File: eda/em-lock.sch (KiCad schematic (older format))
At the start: 47 parts, among them P1 EXT_LED_CONN, P2 RC522A, P3 RC522B, P4 BTN_OPEN, P5 BTN_CALL, P6 ESP8266_CONN, P7 LOCK_CONN, Q1 MMBT3906, Q2 MMBT3906, Q3 MMBT3906, Q4 Q_NMOS_DGS, U1 74LVC2G14

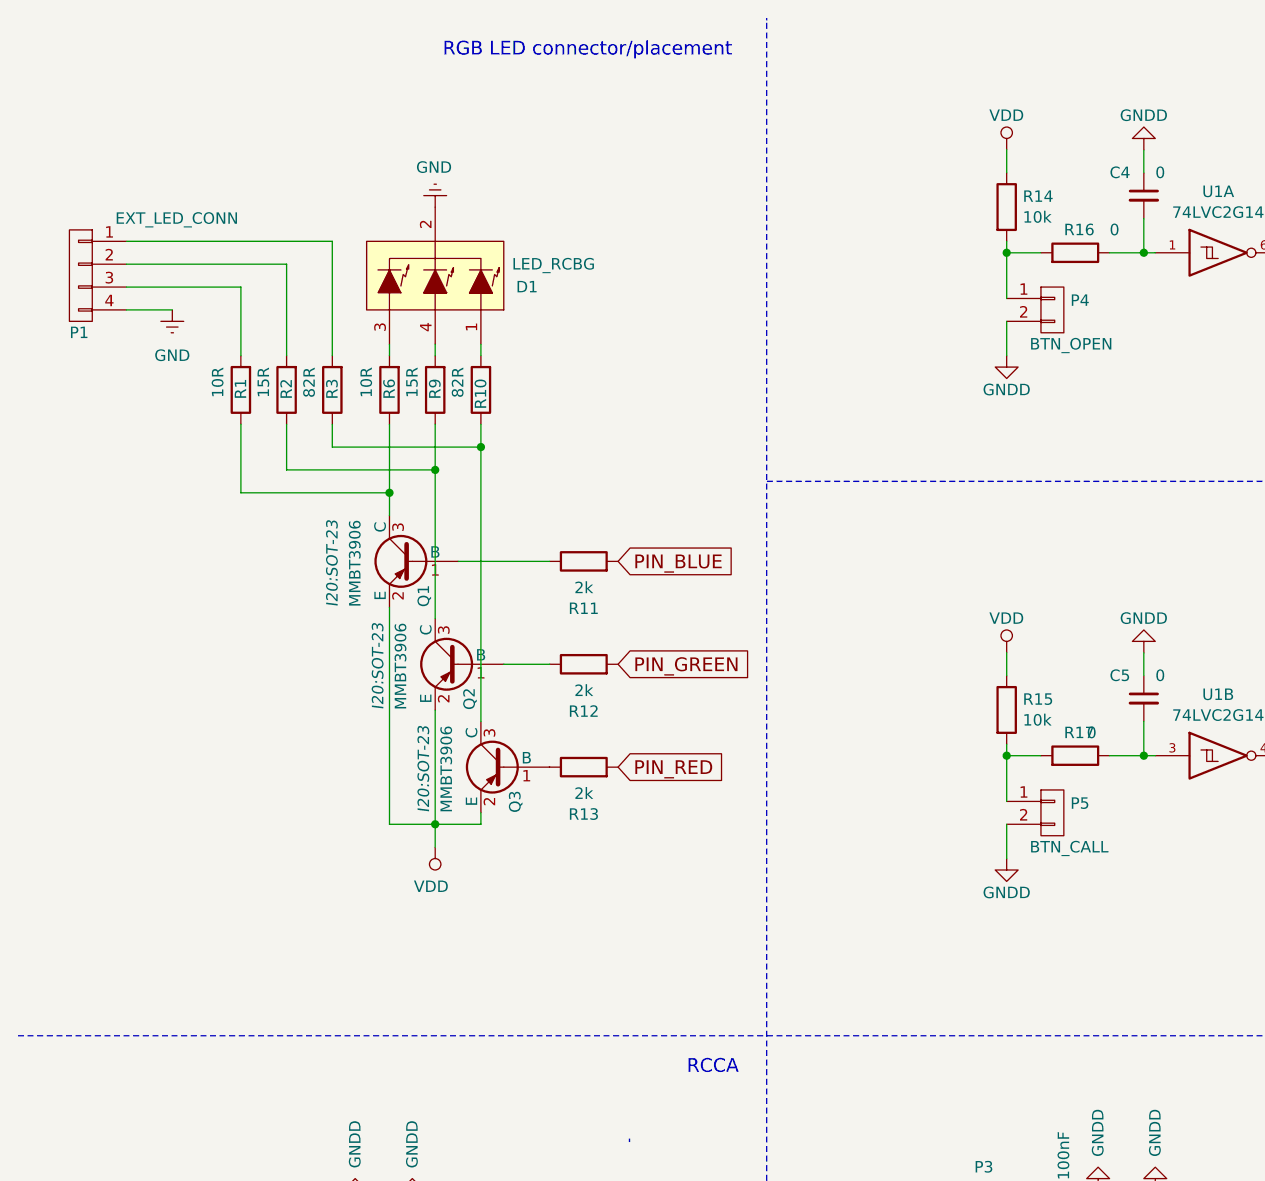
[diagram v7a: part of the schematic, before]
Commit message: refs #41563 rc522 moved up, RGB LEDs moved to separate pcbs, 3d model of rc522 implemented.
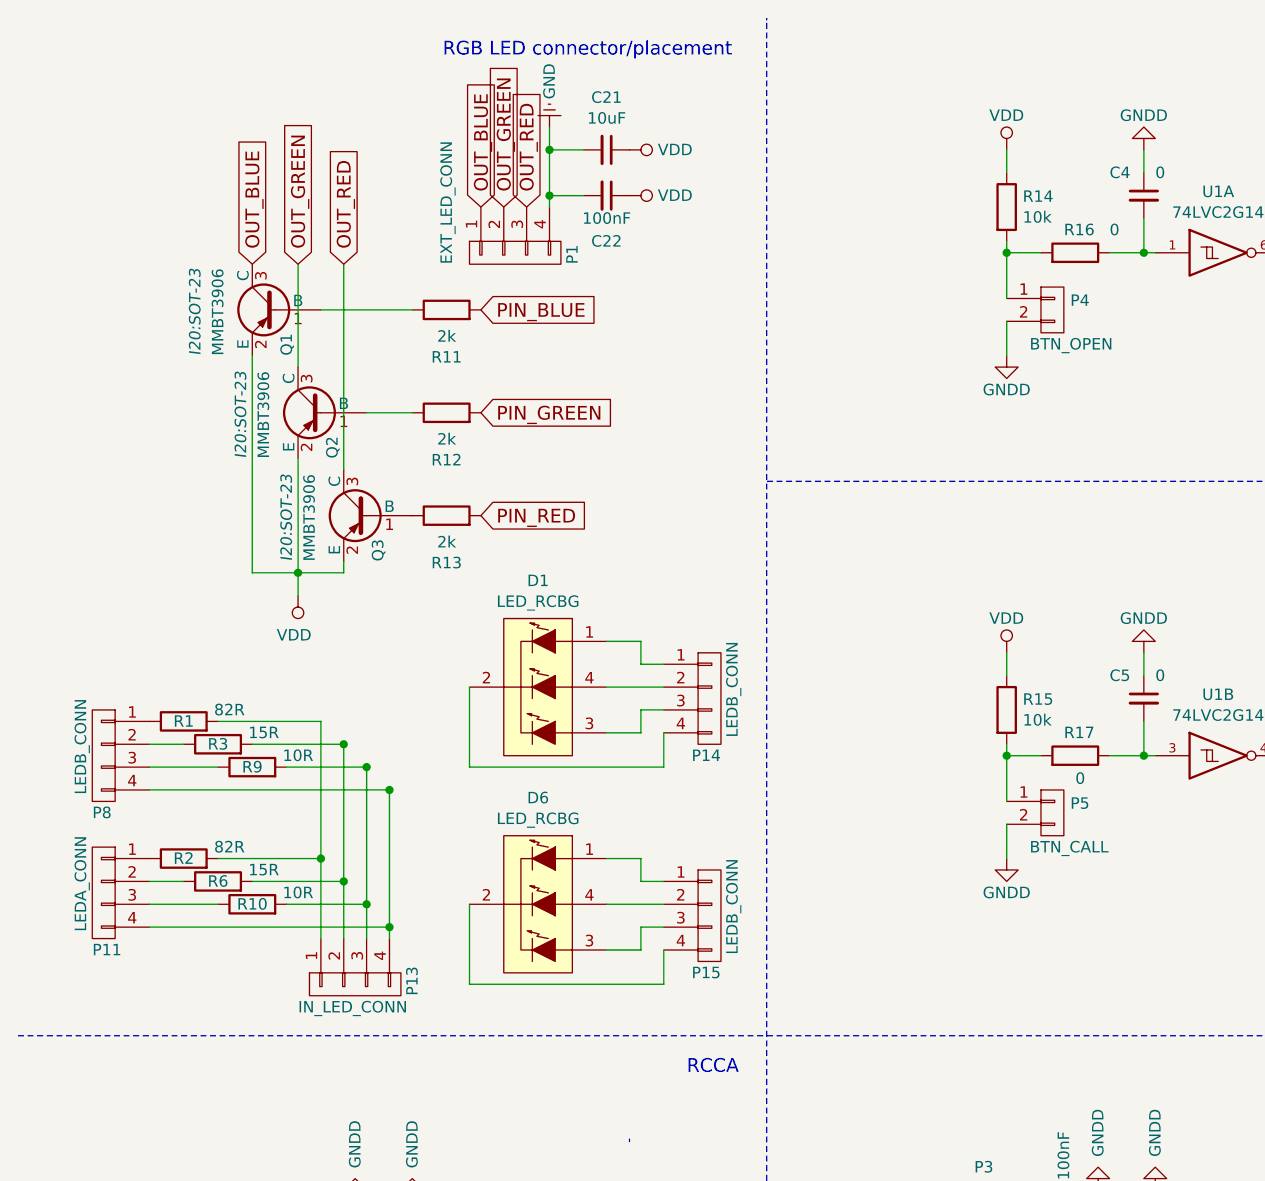
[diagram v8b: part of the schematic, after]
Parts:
- added C21: 10uF, I20:C_0805, symbol C_Small
- added C22: 100nF, I20:C_0805, symbol C_Small
- added D6: LED_RCBG, I20:LED-RGB-5MM_Common_Cathode, symbol LED_RCBG
- added P11: LEDA_CONN, I20:jst-s4b-ph-kl-angled, symbol CONN_01X04
- added P13: IN_LED_CONN, I20:jst-s4b-ph-kl-angled, symbol CONN_01X04
- added P14, P15, P8: LEDB_CONN, I20:jst-s4b-ph-kl-angled, symbol CONN_01X04
- P2: footprint Pin_Headers:Pin_Header_Straight_1x08 -> I20:RC522_Full
- P6: footprint I20:ESP8266_CONN -> I20:ESP8266
- R1: value 10R -> 82R
- R10: value 82R -> 10R
- R2: value 15R -> 82R
- R3: value 82R -> 15R
- R6: value 10R -> 15R
- R9: value 15R -> 10R
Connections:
- net GNDREF: now also C21.2, C22.2; no longer D1.2 (COMMON_CATHODE)
- net VDD: now also C21.1, C22.1
- net at R10.2: now also R9.2, P13.3 (P3); no longer D1.1 (RED_ANODE)
- net at R6.2: now also R3.2, P13.2 (P2); no longer D1.3 (BLUE_ANODE)
- net at D1.4 (GREEN_ANODE): now also P14.2 (P2); no longer R9.2
- net OUT_BLUE: now reaches P1.1 (P1)
- net OUT_BLUE: now also Q1.3 (C); no longer R3.2
- net at R2.2: now also R1.2, P13.1 (P1); no longer P1.2 (P2)
- net OUT_RED: now reaches P1.3 (P3)
- net OUT_RED: now also Q3.3 (C); no longer R1.2
- new net: P11.4 (P4), P13.4 (P4), P8.4 (P4)
- new net: P8.1 (P1), R1.1
- new net: P8.2 (P2), R3.1
- new net: P8.3 (P3), R9.1
- new net: P11.1 (P1), R2.1
- new net: P11.2 (P2), R6.1
- new net: P11.3 (P3), R10.1
- new net: D6.1 (RED_ANODE), P15.1 (P1)
- new net: D6.2 (COMMON_CATHODE), P15.4 (P4)
- new net: D6.3 (BLUE_ANODE), P15.3 (P3)
- new net: D6.4 (GREEN_ANODE), P15.2 (P2)
- new net: D1.1 (RED_ANODE), P14.1 (P1)
- new net: D1.2 (COMMON_CATHODE), P14.4 (P4)
- new net: D1.3 (BLUE_ANODE), P14.3 (P3)
- new net OUT_GREEN: P1.2 (P2), Q2.3 (C)
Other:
- moved on the sheet: P1, Q1, Q2, Q3, R11, R12, R13
